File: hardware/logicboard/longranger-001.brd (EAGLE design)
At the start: 36 x 72 mm, 25 parts, among them IC1 74ALS05N, IC2 LTC485N, IC3 LTC485N

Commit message: Changed copyright notice.
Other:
- board text added: "MIDI Longranger 1.0.0 by Pineapple Design"
- board text removed: "MIDI Longranger 1.0.0 by Pineapple Computer"
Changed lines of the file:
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@@
 <hole x="33" y="69" drill="3.2"/>
 <hole x="3" y="69" drill="3.2"/>
-<text x="6.35" y="68.58" size="0.8128" layer="25">MIDI Longranger 1.0.0 by Pineapple Computer</text>
+<text x="6.35" y="68.58" size="0.8128" layer="25">MIDI Longranger 1.0.0 by Pineapple Design</text>
 <text x="30.48" y="52.07" size="0.8128" layer="25">MIDI OUT</text>
 <text x="30.48" y="7.62" size="0.8128" layer="25">MIDI IN</text>

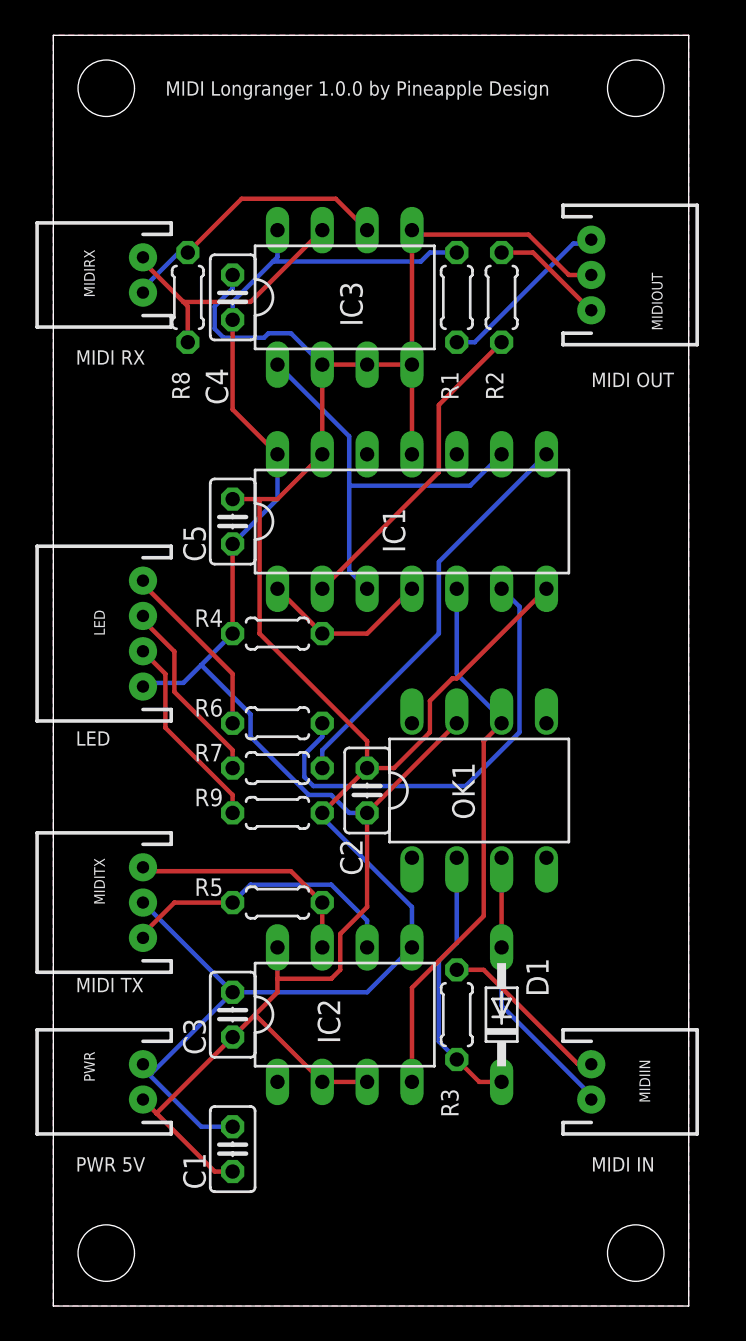
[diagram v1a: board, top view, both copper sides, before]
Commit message: Changed LED pitch.
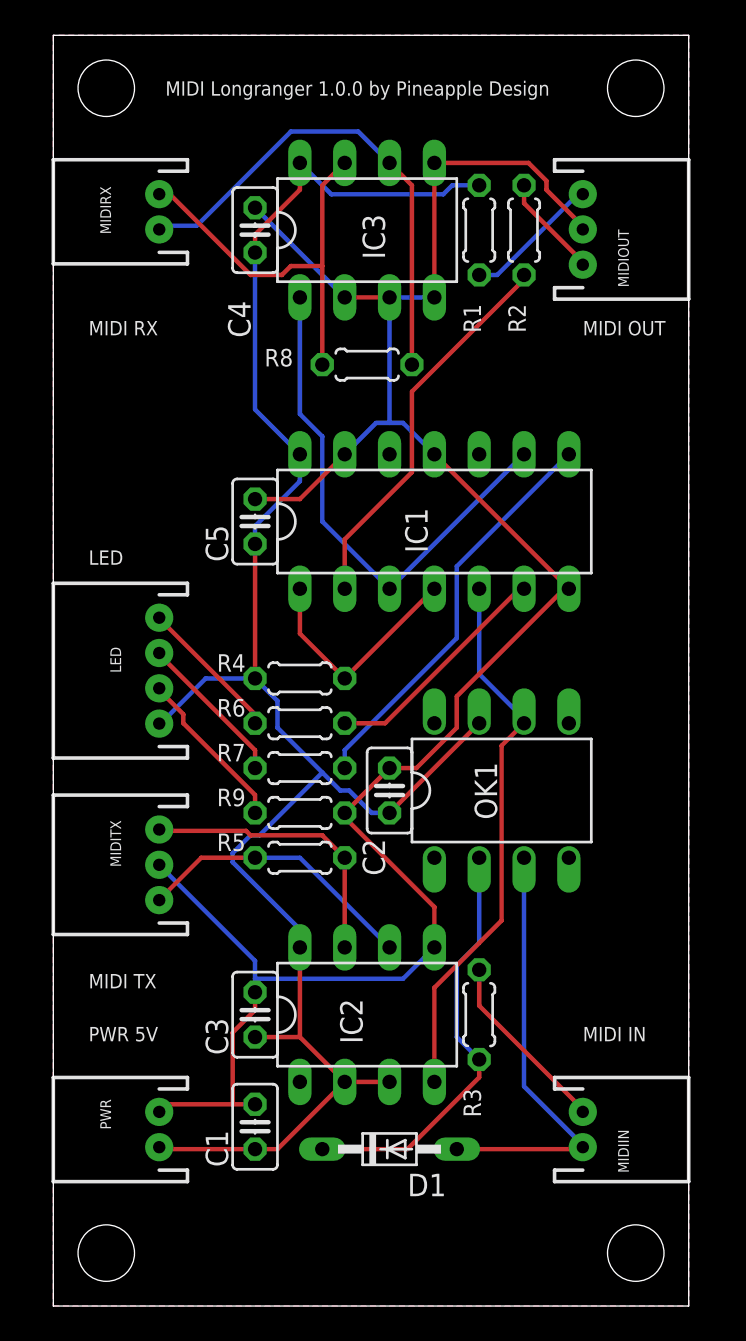
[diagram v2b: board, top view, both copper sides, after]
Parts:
- moved R8 10.9 mm to (17.8, 53.3), turned to 0 degrees
- moved D1 9.92 mm to (19.1, 8.89), turned to 0 degrees
- moved R2 4.02 mm to (26.7, 61.0)
- moved C4 4.02 mm to (11.4, 61.0)
- moved IC3 4.02 mm to (17.8, 61.0)
- moved R1 4.02 mm to (24.1, 61.0)
- moved MIDIRX 3.70 mm to (6.00, 62.0)
- moved PWR 2.85 mm to (6.00, 10.0)
- moved R4 2.84 mm to (14.0, 35.6)
- moved R5 2.84 mm to (14.0, 25.4)
- moved MIDIIN 2.74 mm to (30.0, 10.0)
- moved MIDIOUT 2.62 mm to (30.0, 61.0)
- moved MIDITX 2.33 mm to (6.00, 25.0)
- moved LED 2.29 mm to (6.00, 36.0)
- moved C1 1.80 mm to (11.4, 10.2)
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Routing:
- net N$6: track 25.7 -> 13.3 mm
- net RX+: track 15.8 -> 28.1 mm
- net MIDIRX-: track 15.8 -> 25.0 mm
- net N$15: track 15.3 -> 24.1 mm
- net RX-: track 15.4 -> 23.3 mm
- net GND: track 129.6 -> 122.4 mm
- net N$1: track 24.2 -> 29.4 mm
- net VCC: track 104.1 -> 108.6 mm
- net N$2: track 18.2 -> 22.0 mm
- net N$3: track 9.72 -> 13.3 mm
- net TX-: track 13.7 -> 16.2 mm
- net MIDITX+: track 10.2 -> 8.09 mm
- net N$10: track 11.3 -> 9.29 mm
- net N$9: track 10.7 -> 8.75 mm
- net N$8: track 10.2 -> 8.22 mm
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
